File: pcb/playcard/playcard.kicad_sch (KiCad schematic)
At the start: 9 parts, among them SW1 SW_MEC_5E, SW2 SW_MEC_5E, SW3 SW_MEC_5E, SW4 SW_MEC_5E, SW5 SW_MEC_5E, SW6 SW_MEC_5E, U1 BlackPill_Part_Like_SWD_Break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, U3 2.4_TFT_ILI9341, U4 ESP32-S3-ZERO

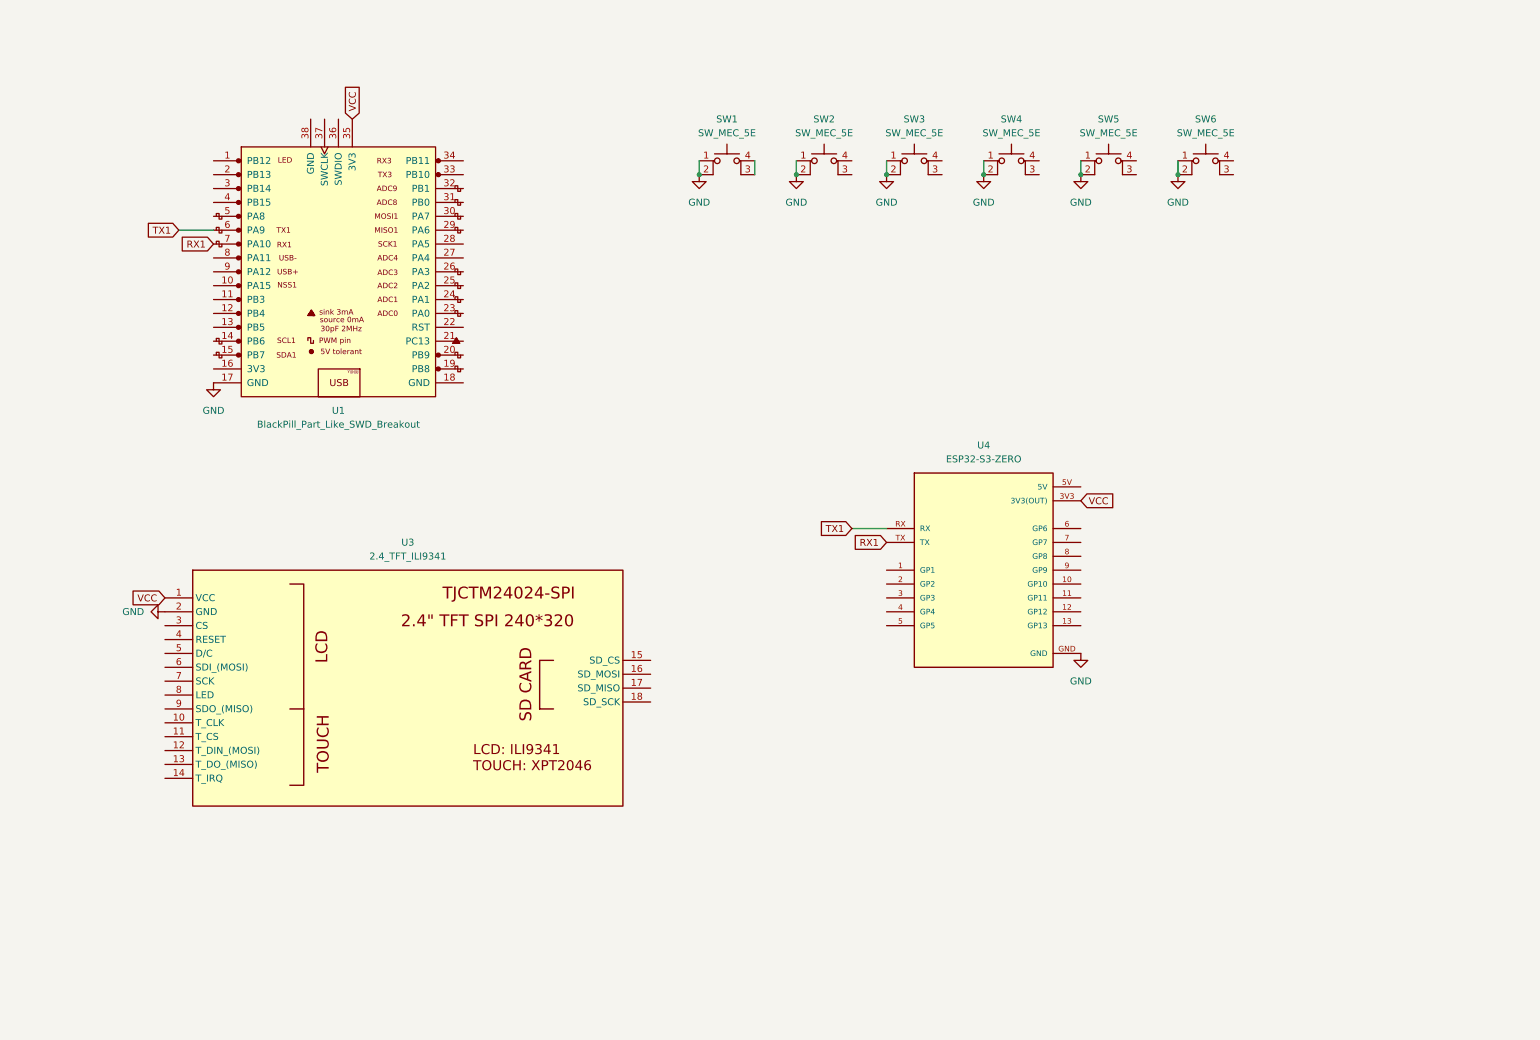
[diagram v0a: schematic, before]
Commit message: updated pcb and readme
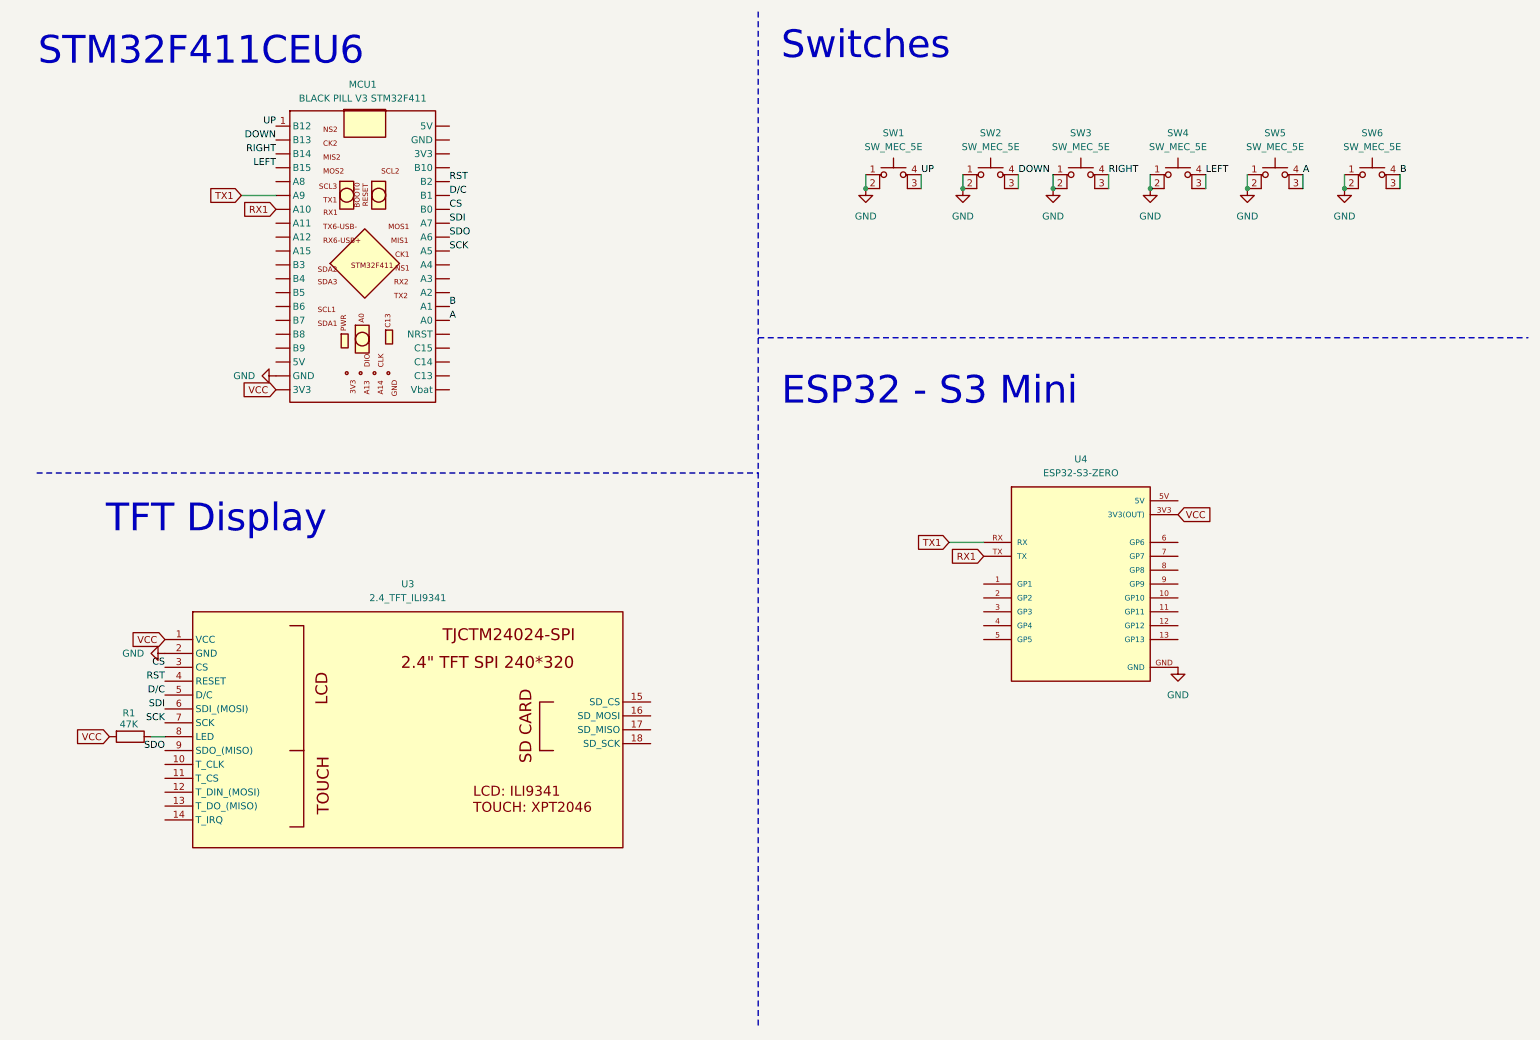
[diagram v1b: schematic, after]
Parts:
- removed U1: BlackPill_Part_Like_SWD_Breakout, MCU_personal:BlackPill_SWD_2, symbol MCU_personal:STM_BlackPill_Part_Like_SWD_Breakout
- added MCU1: BLACK PILL V3 STM32F411, MCU_personal:BLACK PILL V3, symbol MCU_personal:BLACK PILL V3 STM32F411
- added R1: 47K, Resistor_SMD:R_0612_1632Metric, symbol Device:R
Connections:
- net GND: now also MCU1.19 (GND)
- net RX1: now also MCU1.7 (A10)
- net TX1: now also MCU1.6 (A9)
- net VCC: now also MCU1.20 (3V3), R1.2
- net B: now reaches SW6.3 (K)
- net B: now also SW6.4 (A), MCU1.34 (A1)
- net UP: now reaches SW1.3 (K), SW1.4 (A)
- net UP: now also MCU1.1 (B12)
- net A: now reaches SW5.3 (K)
- net A: now also SW5.4 (A), MCU1.35 (A0)
- net LEFT: now reaches SW4.3 (K)
- net LEFT: now also SW4.4 (A), MCU1.4 (B15)
- net DOWN: now reaches SW2.3 (K)
- net DOWN: now also SW2.4 (A), MCU1.2 (B13)
- net CS: now reaches U3.3 (CS)
- net CS: now also MCU1.27 (B0)
- net RST: now reaches U3.4 (RESET)
- net RST: now also MCU1.25 (B2)
- net D/C: now reaches U3.5 (D/C)
- net D/C: now also MCU1.26 (B1)
- net SDI: now reaches U3.6 (SDI_(MOSI))
- net SDI: now also MCU1.28 (A7)
- net SCK: now reaches U3.7 (SCK)
- net SCK: now also MCU1.30 (A5)
- net at U3.8 (LED): now also R1.1
- net SDO: now reaches U3.9 (SDO_(MISO))
- net SDO: now also MCU1.29 (A6)
- net RIGHT: now reaches SW3.3 (K)
- net RIGHT: now also SW3.4 (A), MCU1.3 (B14)
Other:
- note added: "ESP32 - S3 Mini"
- note added: "STM32F411CEU6"
- note added: "Switches"
- note added: "TFT Display"
- moved on the sheet: SW1, SW2, SW3, SW4, SW5, SW6, U3, U4
